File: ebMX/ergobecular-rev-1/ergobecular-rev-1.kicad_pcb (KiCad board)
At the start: 2 copper layers, 29 parts, among them J3 OLED, U1 ProMicro

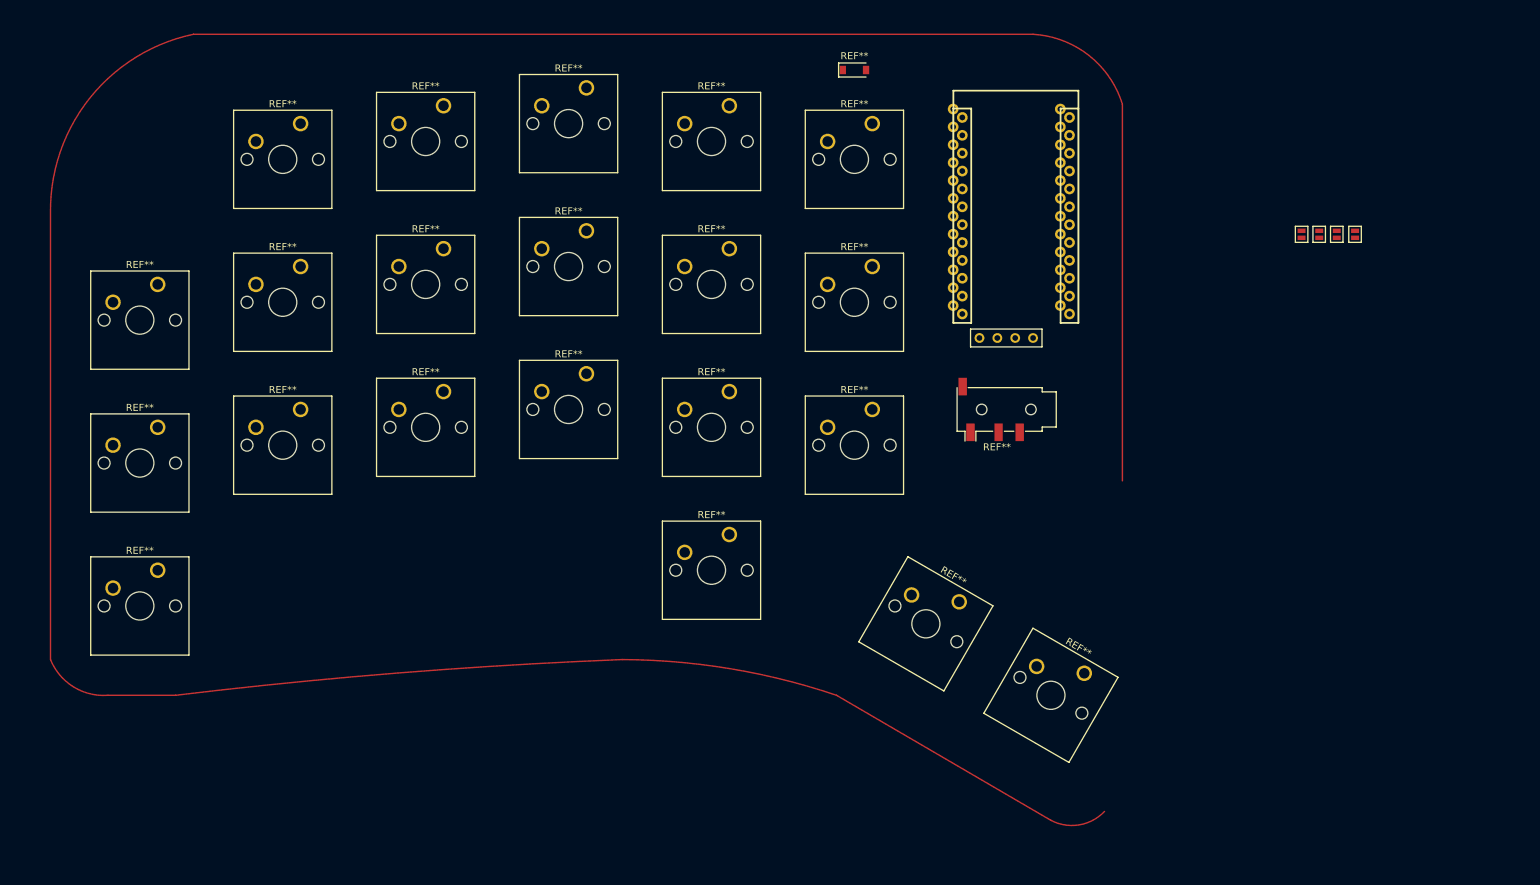
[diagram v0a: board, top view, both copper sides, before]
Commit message: updated brackets on Ergodox
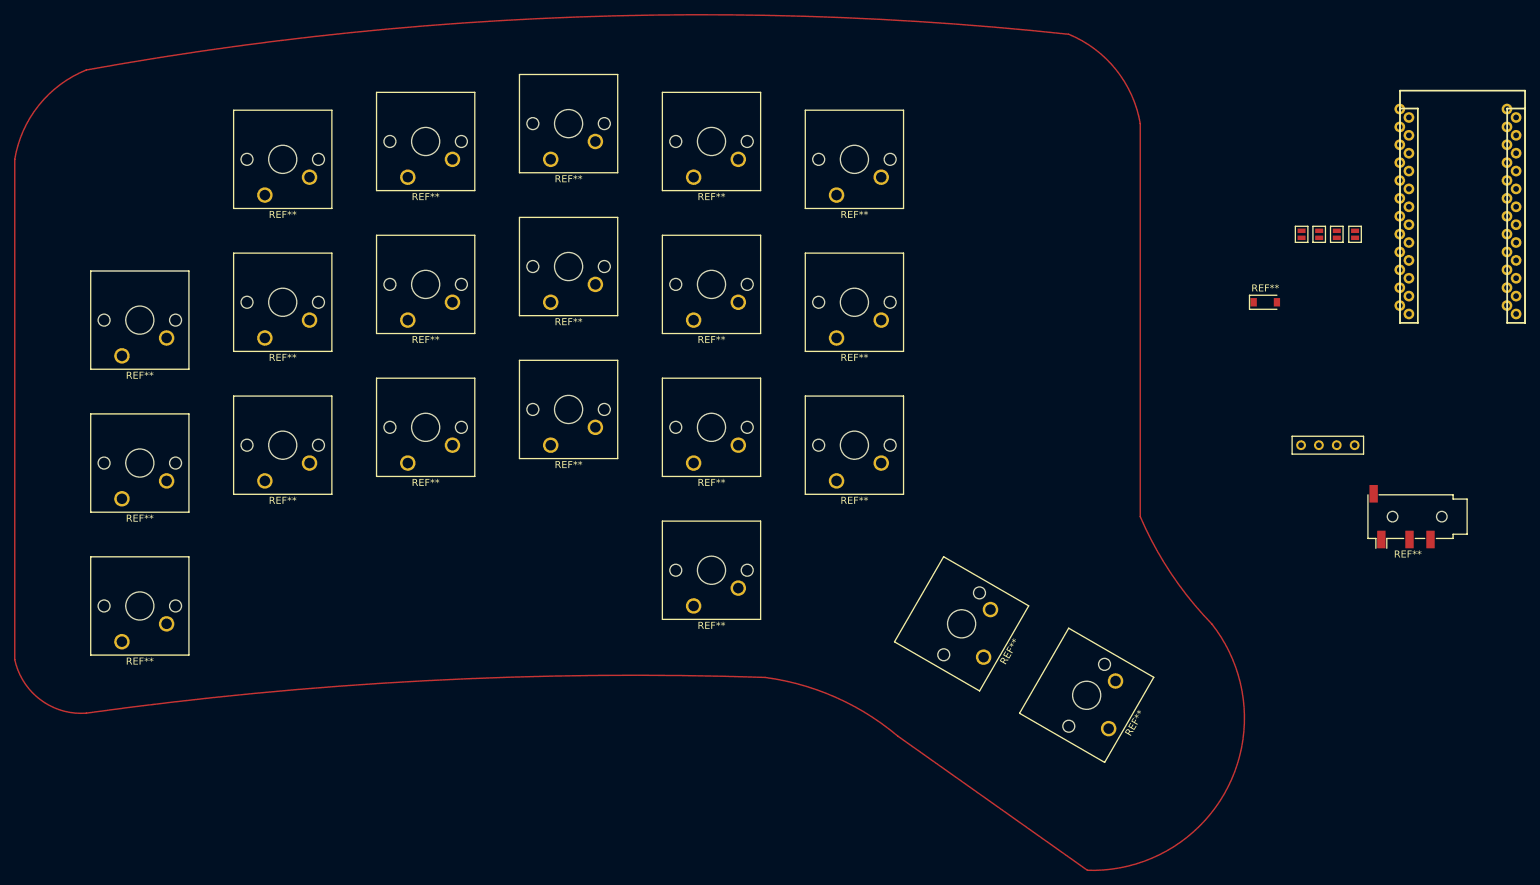
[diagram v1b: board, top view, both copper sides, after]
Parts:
- removed the REF** at (157.1, 123.9)
- removed the REF** at (174.9, 134.0)
- added REF**: SW_Cherry_MX_1.50u_PCB, Button_Switch_Keyboard:SW_Cherry_MX_1.50u_PCB, F.Cu at (178.4, 141.9)
- added REF**: SW_Cherry_MX_1.50u_PCB, Button_Switch_Keyboard:SW_Cherry_MX_1.50u_PCB, F.Cu at (160.6, 131.7)
- moved REF** 71.3 mm to (119.4, 124.5), turned to 180 degrees
- moved REF** 67.1 mm to (200.7, 81.3)
- moved U1 63.5 mm to (228.6, 68.6)
- moved REF** 60.4 mm to (221.0, 111.8)
- moved REF** 51.1 mm to (139.7, 106.7), turned to 180 degrees
- moved REF** 51.1 mm to (119.4, 63.5), turned to 180 degrees
- moved REF** 51.1 mm to (78.7, 104.1), turned to 180 degrees
- moved REF** 51.1 mm to (99.1, 101.6), turned to 180 degrees
- moved J3 48.2 mm to (205.7, 101.6)
- moved REF** 30.9 mm to (119.4, 104.1), turned to 180 degrees
- moved REF** 30.9 mm to (78.7, 63.5), turned to 180 degrees
- moved REF** 30.9 mm to (58.4, 106.7), turned to 180 degrees
- moved REF** 30.9 mm to (99.1, 61.0), turned to 180 degrees
- moved REF** 30.9 mm to (139.7, 66.0), turned to 180 degrees
- moved REF** 11.4 mm to (119.4, 83.8), turned to 180 degrees
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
